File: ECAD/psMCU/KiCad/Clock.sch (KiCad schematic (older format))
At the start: 0 parts

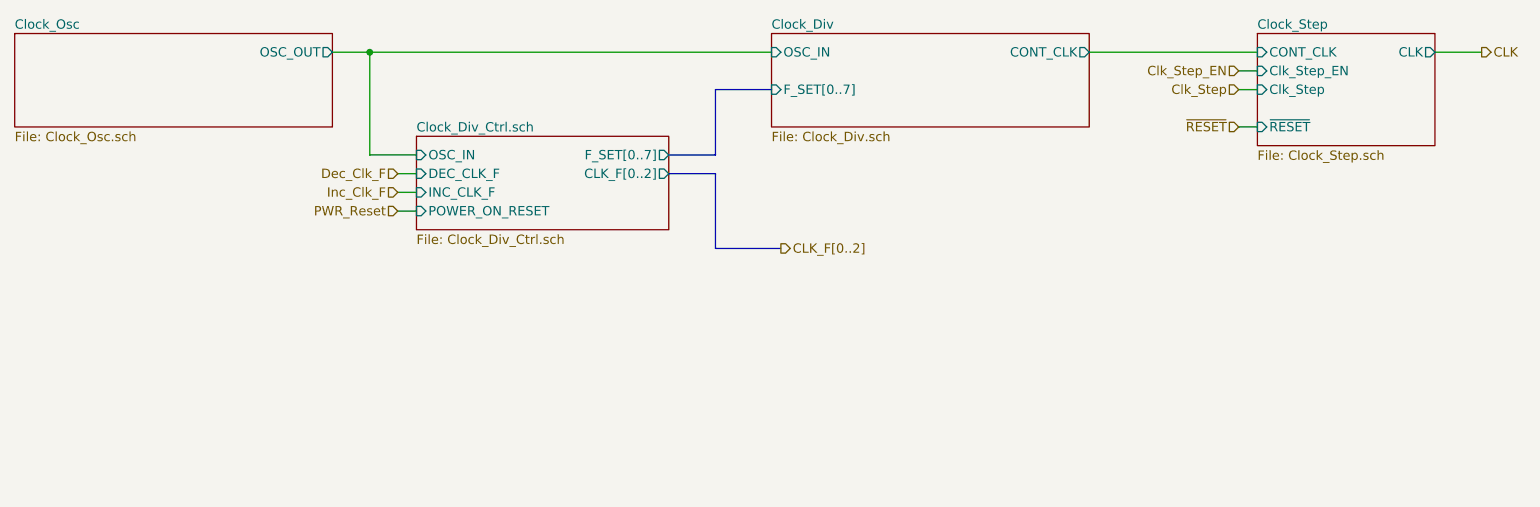
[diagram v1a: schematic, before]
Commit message: Sch: Improved Clk/Reset distribution, moved to global labels
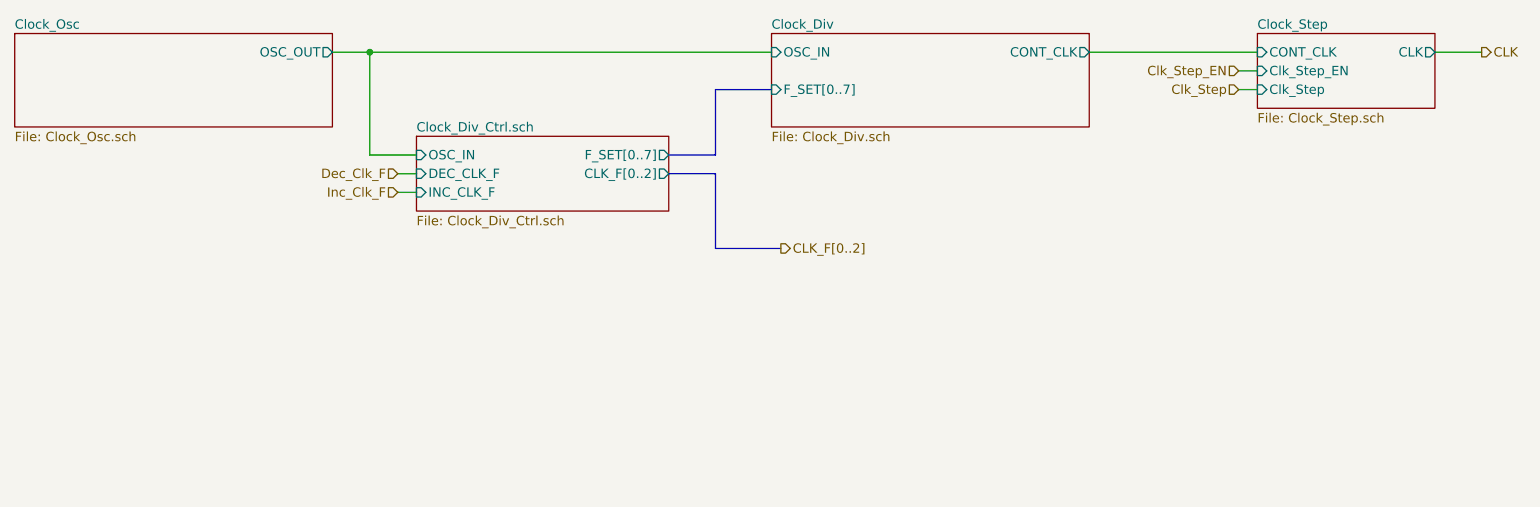
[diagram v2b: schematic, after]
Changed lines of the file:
@@
 $Descr A4 11693 8268
 encoding utf-8
-Sheet 63 96
+Sheet 61 97
 Title "psMCU"
 Date "2022-02-13"
@@
 Comment4 "Variable frequency clock generation."
 $EndDescr
-Text HLabel 8450 2250 0    50   Input ~ 0
-Clk_Step_EN
-Text HLabel 8450 2350 0    50   Input ~ 0
-Clk_Step
-Text HLabel 3950 2900 0    50   Input ~ 0
-Inc_Clk_F
-Text HLabel 3950 2800 0    50   Input ~ 0
-Dec_Clk_F
-$Sheet
-S 8550 2050 950  600
-U 5FFAAF6D
-F0 "Clock_Step" 50
-F1 "Clock_Step.sch" 50
-F2 "CLK" O R 9500 2150 50
-F3 "CONT_CLK" I L 8550 2150 50
-F4 "~RESET" I L 8550 2550 50
-F5 "Clk_Step_EN" I L 8550 2250 50
-F6 "Clk_Step" I L 8550 2350 50
-$EndSheet
-$Sheet
-S 1900 2050 1700 500
-U 5FFC76CA
-F0 "Clock_Osc" 50
-F1 "Clock_Osc.sch" 50
-F2 "OSC_OUT" O R 3600 2150 50
-$EndSheet
-Text HLabel 9750 2150 2    50   Output ~ 0
-CLK
+Text HLabel 6000 3200 2    50   Output ~ 0
+CLK_F[0..2]
+Wire Bus Line
+	5650 3200 6000 3200
+Wire Bus Line
+	5650 2800 5650 3200
+Wire Bus Line
+	5400 2800 5650 2800
+Wire Bus Line
+	5650 2350 5950 2350
+Wire Bus Line
+	5650 2700 5650 2350
+Wire Bus Line
+	5400 2700 5650 2700
 Wire Wire Line
-	9750 2150 9500 2150
+	3800 2150 5950 2150
+Connection ~ 3800 2150
 Wire Wire Line
-	8450 2250 8550 2250
+	3800 2700 3800 2150
 Wire Wire Line
-	8450 2350 8550 2350
+	3600 2150 3800 2150
 Wire Wire Line
-	3950 2800 4050 2800
-Wire Wire Line
-	4050 2900 3950 2900
-Text HLabel 3950 3000 0    50   Input ~ 0
-PWR_Reset
-$Sheet
-S 4050 2600 1350 500
-U 60010AFF
-F0 "Clock_Div_Ctrl.sch" 50
-F1 "Clock_Div_Ctrl.sch" 50
-F2 "INC_CLK_F" I L 4050 2900 50
-F3 "DEC_CLK_F" I L 4050 2800 50
-F4 "OSC_IN" I L 4050 2700 50
-F5 "POWER_ON_RESET" I L 4050 3000 50
-F6 "F_SET[0..7]" O R 5400 2700 50
-F7 "CLK_F[0..2]" O R 5400 2800 50
-$EndSheet
-Wire Wire Line
-	3950 3000 4050 3000
-Wire Wire Line
-	3800 2700 4050 2700
+	7650 2150 8550 2150
 $Sheet
 S 5950 2050 1700 500
@@
 $EndSheet
 Wire Wire Line
-	7650 2150 8550 2150
+	3800 2700 4050 2700
+$Sheet
+S 4050 2600 1350 400
+U 60010AFF
+F0 "Clock_Div_Ctrl.sch" 50
+F1 "Clock_Div_Ctrl.sch" 50
+F2 "INC_CLK_F" I L 4050 2900 50
+F3 "DEC_CLK_F" I L 4050 2800 50
+F4 "OSC_IN" I L 4050 2700 50
+F6 "F_SET[0..7]" O R 5400 2700 50
+F7 "CLK_F[0..2]" O R 5400 2800 50
+$EndSheet
 Wire Wire Line
-	3600 2150 3800 2150
+	4050 2900 3950 2900
 Wire Wire Line
-	3800 2700 3800 2150
-Connection ~ 3800 2150
+	3950 2800 4050 2800
 Wire Wire Line
-	3800 2150 5950 2150
-Wire Bus Line
-	5400 2700 5650 2700
-Wire Bus Line
-	5650 2700 5650 2350
-Wire Bus Line
-	5650 2350 5950 2350
-Text HLabel 8450 2550 0    50   Input ~ 0
-~RESET
+	8450 2350 8550 2350
 Wire Wire Line
-	8450 2550 8550 2550
-Wire Bus Line
-	5400 2800 5650 2800
-Wire Bus Line
-	5650 2800 5650 3200
-Wire Bus Line
-	5650 3200 6000 3200
-Text HLabel 6000 3200 2    50   Output ~ 0
-CLK_F[0..2]
+	8450 2250 8550 2250
+Wire Wire Line
+	9750 2150 9500 2150
+$Sheet
+S 1900 2050 1700 500
+U 5FFC76CA
+F0 "Clock_Osc" 50
+F1 "Clock_Osc.sch" 50
+F2 "OSC_OUT" O R 3600 2150 50
+$EndSheet
+$Sheet
+S 8550 2050 950  400
+U 5FFAAF6D
+F0 "Clock_Step" 50
+F1 "Clock_Step.sch" 50
+F2 "CLK" O R 9500 2150 50
+F3 "CONT_CLK" I L 8550 2150 50
+F5 "Clk_Step_EN" I L 8550 2250 50
+F6 "Clk_Step" I L 8550 2350 50
+$EndSheet
+Text HLabel 3950 2800 0    50   Input ~ 0
+Dec_Clk_F
+Text HLabel 3950 2900 0    50   Input ~ 0
+Inc_Clk_F
+Text HLabel 8450 2350 0    50   Input ~ 0
+Clk_Step
+Text HLabel 8450 2250 0    50   Input ~ 0
+Clk_Step_EN
+Text HLabel 9750 2150 2    50   Output ~ 0
+CLK
 $EndSCHEMATC

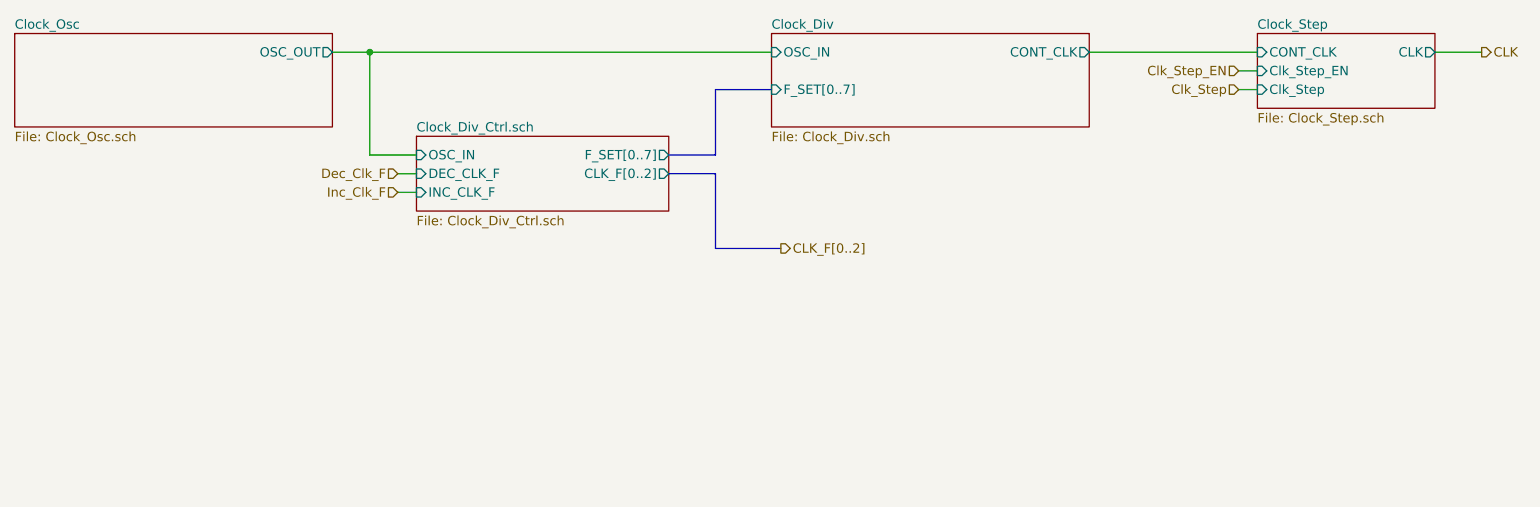
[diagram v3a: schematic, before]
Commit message: Sch: Changed Clock Stepping to be simpler and more robust.
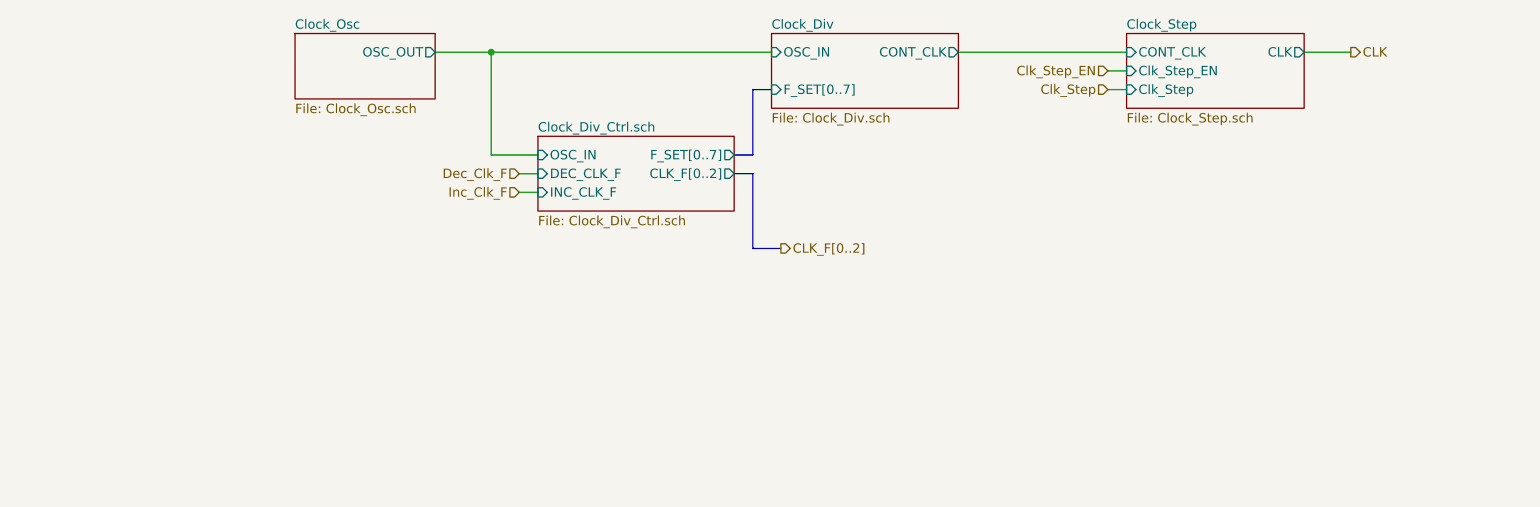
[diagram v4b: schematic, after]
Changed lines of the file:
@@
 $Descr A4 11693 8268
 encoding utf-8
-Sheet 64 102
+Sheet 63 102
 Title "psMCU"
 Date "2022-02-13"
@@
 CLK_F[0..2]
 Wire Bus Line
-	5650 3200 6000 3200
+	5850 2800 5850 3200
 Wire Bus Line
-	5650 2800 5650 3200
-Wire Bus Line
-	5400 2800 5650 2800
-Wire Bus Line
-	5650 2350 5950 2350
-Wire Bus Line
-	5650 2700 5650 2350
-Wire Bus Line
-	5400 2700 5650 2700
+	5850 2700 5850 2350
 Wire Wire Line
-	3800 2150 5950 2150
-Connection ~ 3800 2150
+	4450 2700 4450 2150
 Wire Wire Line
-	3800 2700 3800 2150
-Wire Wire Line
-	3600 2150 3800 2150
-Wire Wire Line
-	7650 2150 8550 2150
+	6950 2150 7850 2150
 $Sheet
-S 5950 2050 1700 500
+S 5950 2050 1000 400
 U 5FFB4D29
 F0 "Clock_Div" 50
 F1 "Clock_Div.sch" 50
 F2 "OSC_IN" I L 5950 2150 50
-F3 "CONT_CLK" O R 7650 2150 50
+F3 "CONT_CLK" O R 6950 2150 50
 F4 "F_SET[0..7]" I L 5950 2350 50
 $EndSheet
 Wire Wire Line
-	3800 2700 4050 2700
+	4450 2700 4700 2700
 $Sheet
-S 4050 2600 1350 400
+S 4700 2600 1050 400
 U 60010AFF
 F0 "Clock_Div_Ctrl.sch" 50
 F1 "Clock_Div_Ctrl.sch" 50
-F2 "INC_CLK_F" I L 4050 2900 50
-F3 "DEC_CLK_F" I L 4050 2800 50
-F4 "OSC_IN" I L 4050 2700 50
-F5 "F_SET[0..7]" O R 5400 2700 50
-F6 "CLK_F[0..2]" O R 5400 2800 50
+F2 "INC_CLK_F" I L 4700 2900 50
+F3 "DEC_CLK_F" I L 4700 2800 50
+F4 "OSC_IN" I L 4700 2700 50
+F5 "F_SET[0..7]" O R 5750 2700 50
+F6 "CLK_F[0..2]" O R 5750 2800 50
 $EndSheet
 Wire Wire Line
-	4050 2900 3950 2900
+	4700 2900 4600 2900
 Wire Wire Line
-	3950 2800 4050 2800
+	4600 2800 4700 2800
 Wire Wire Line
-	8450 2350 8550 2350
+	7750 2350 7850 2350
 Wire Wire Line
-	8450 2250 8550 2250
+	7750 2250 7850 2250
 Wire Wire Line
-	9750 2150 9500 2150
+	9050 2150 8800 2150
 $Sheet
-S 1900 2050 1700 500
+S 3400 2050 750  350
 U 5FFC76CA
 F0 "Clock_Osc" 50
 F1 "Clock_Osc.sch" 50
-F2 "OSC_OUT" O R 3600 2150 50
+F2 "OSC_OUT" O R 4150 2150 50
 $EndSheet
 $Sheet
-S 8550 2050 950  400
+S 7850 2050 950  400
 U 5FFAAF6D
 F0 "Clock_Step" 50
 F1 "Clock_Step.sch" 50
-F2 "CLK" O R 9500 2150 50
-F3 "CONT_CLK" I L 8550 2150 50
-F4 "Clk_Step_EN" I L 8550 2250 50
-F5 "Clk_Step" I L 8550 2350 50
+F2 "CLK" O R 8800 2150 50
+F3 "CONT_CLK" I L 7850 2150 50
+F4 "Clk_Step_EN" I L 7850 2250 50
+F5 "Clk_Step" I L 7850 2350 50
 $EndSheet
-Text HLabel 3950 2800 0    50   Input ~ 0
+Text HLabel 4600 2800 0    50   Input ~ 0
 Dec_Clk_F
-Text HLabel 3950 2900 0    50   Input ~ 0
+Text HLabel 4600 2900 0    50   Input ~ 0
 Inc_Clk_F
-Text HLabel 8450 2350 0    50   Input ~ 0
+Text HLabel 7750 2350 0    50   Input ~ 0
 Clk_Step
-Text HLabel 8450 2250 0    50   Input ~ 0
+Text HLabel 7750 2250 0    50   Input ~ 0
 Clk_Step_EN
-Text HLabel 9750 2150 2    50   Output ~ 0
+Text HLabel 9050 2150 2    50   Output ~ 0
 CLK
+Wire Wire Line
+	4450 2150 5950 2150
+Wire Bus Line
+	5950 2350 5850 2350
+Wire Bus Line
+	5850 2700 5750 2700
+Wire Bus Line
+	5750 2800 5850 2800
+Wire Bus Line
+	5850 3200 6000 3200
+Wire Wire Line
+	4150 2150 4450 2150
+Connection ~ 4450 2150
 $EndSCHEMATC

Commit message: Sch: Implemented much improved debugger interface
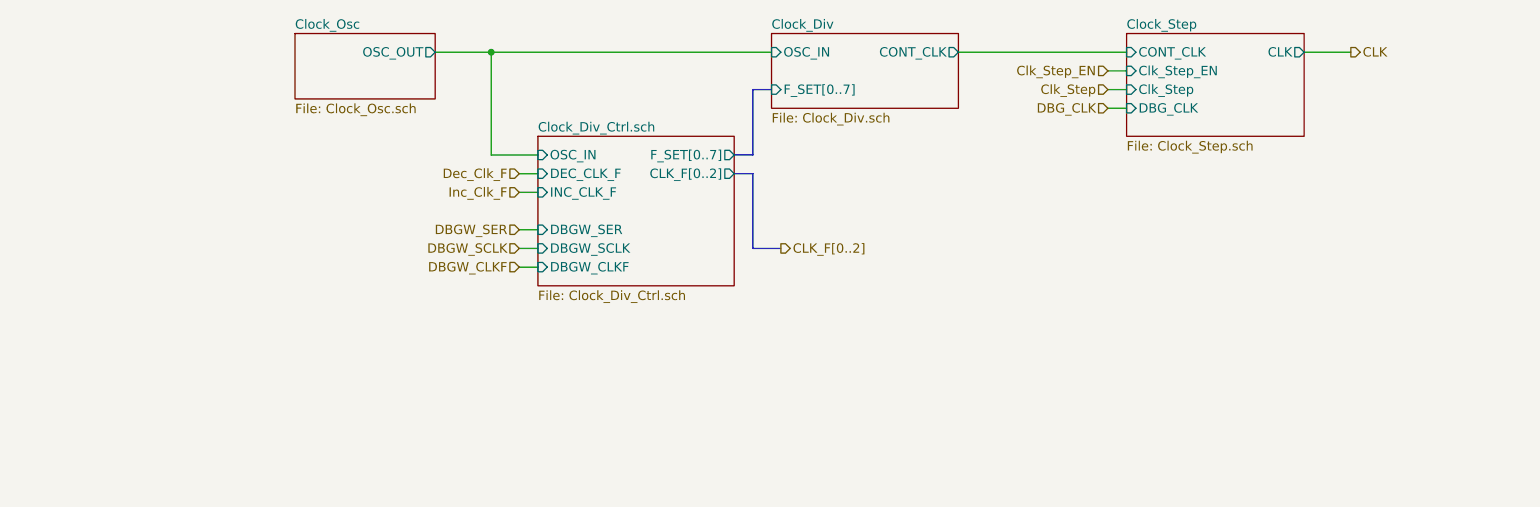
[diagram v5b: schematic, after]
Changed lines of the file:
@@
 $Descr A4 11693 8268
 encoding utf-8
-Sheet 63 102
+Sheet 56 105
 Title "psMCU"
 Date "2022-02-13"
@@
 	4450 2700 4700 2700
 $Sheet
-S 4700 2600 1050 400
+S 4700 2600 1050 800
 U 60010AFF
 F0 "Clock_Div_Ctrl.sch" 50
@@
 F5 "F_SET[0..7]" O R 5750 2700 50
 F6 "CLK_F[0..2]" O R 5750 2800 50
+F7 "DBGW_SER" I L 4700 3100 50
+F8 "DBGW_SCLK" I L 4700 3200 50
+F9 "DBGW_CLKF" I L 4700 3300 50
 $EndSheet
 Wire Wire Line
@@
 $EndSheet
 $Sheet
-S 7850 2050 950  400
+S 7850 2050 950  550
 U 5FFAAF6D
 F0 "Clock_Step" 50
@@
 F4 "Clk_Step_EN" I L 7850 2250 50
 F5 "Clk_Step" I L 7850 2350 50
+F6 "DBG_CLK" I L 7850 2450 50
 $EndSheet
 Text HLabel 4600 2800 0    50   Input ~ 0
@@
 	4150 2150 4450 2150
 Connection ~ 4450 2150
+Text HLabel 7750 2450 0    50   Input ~ 0
+DBG_CLK
+Wire Wire Line
+	7850 2450 7750 2450
+Wire Wire Line
+	4700 3100 4600 3100
+Wire Wire Line
+	4700 3200 4600 3200
+Wire Wire Line
+	4700 3300 4600 3300
+Text HLabel 4600 3100 0    50   Input ~ 0
+DBGW_SER
+Text HLabel 4600 3200 0    50   Input ~ 0
+DBGW_SCLK
+Text HLabel 4600 3300 0    50   Input ~ 0
+DBGW_CLKF
 $EndSCHEMATC
